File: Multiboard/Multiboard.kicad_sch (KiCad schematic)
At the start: 51 parts, among them J1 Conn_01x20_Socket, J2 Conn_01x20_Socket, J3 Debug, J4 USB_C_Receptacle_USB2.0_16P, SW1 BOOT0, SW2 NRST, SW8 KEY, U1 STM32F411RET6, U2 MAX662AESA_T, U3 MCP1792x-3302xCB, Y1 32.768KHz, Y2 25MHz

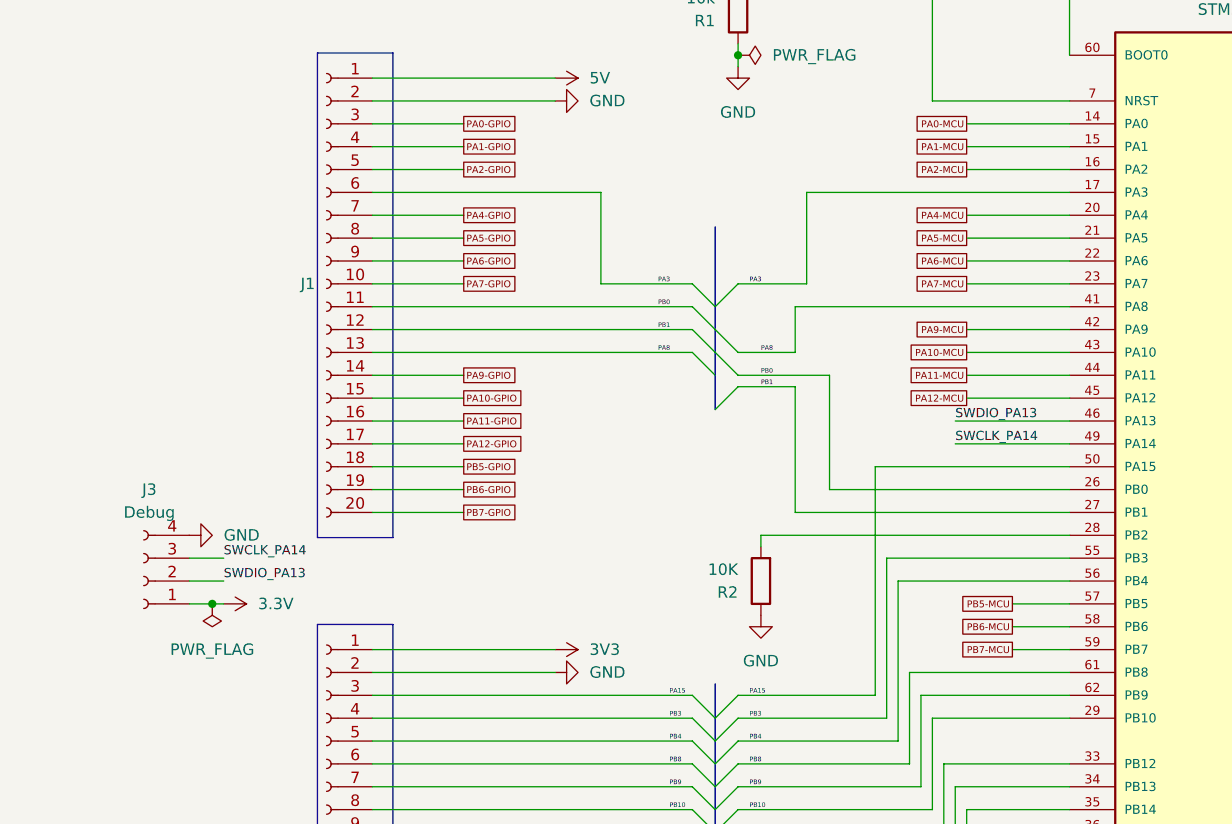
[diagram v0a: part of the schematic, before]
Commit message: FIxed level shifter implementation
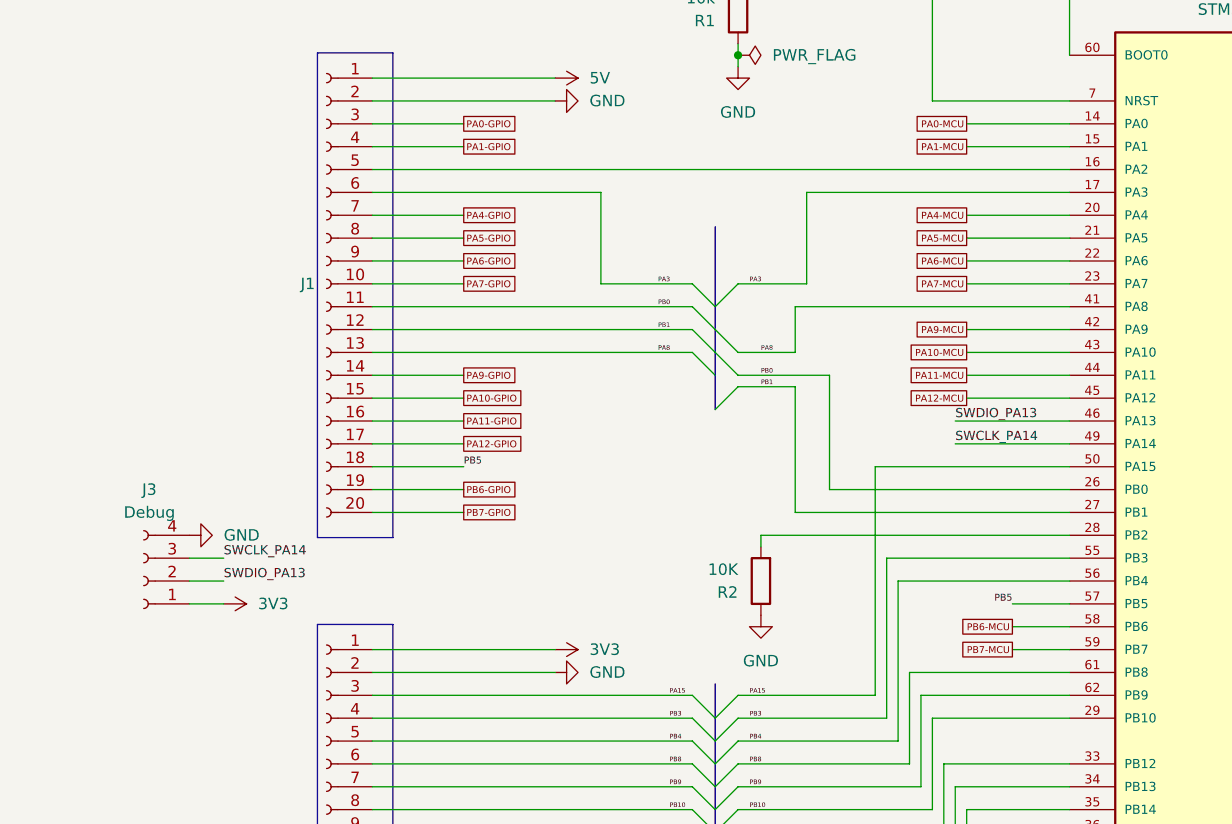
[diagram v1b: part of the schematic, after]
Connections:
- net 3.3V is gone; now on net 3V3: J3.1 (Pin_1)
- net PA2-MCU is gone; now on an unnamed net: U1.16 (PA2)
- net PB5-MCU is gone; now on net PB5: U1.57 (PB5)
- net PA2-GPIO: no longer names the net of J1.5 (Pin_5)
- net PB5-GPIO renamed PB5
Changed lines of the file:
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@@
 	)
 	(junction
-		(at 57.15 123.19)
-		(diameter 0)
-		(color 0 0 0 0)
-	)
-	(junction
 		(at 261.62 83.82)
 		(diameter 0)
@@
 	(wire
 		(pts
-			(xy 74.93 74.93) (xy 85.09 74.93)
+			(xy 74.93 74.93) (xy 152.4 74.93)
 		)
 		(stroke
@@
 	(wire
 		(pts
-			(xy 57.15 123.19) (xy 54.61 123.19)
-		)
-		(stroke
-			(width 0)
-			(type default)
-		)
-	)
-	(wire
-		(pts
 			(xy 74.93 97.79) (xy 85.09 97.79)
 		)
@@
 	(wire
 		(pts
-			(xy 58.42 123.19) (xy 57.15 123.19)
+			(xy 54.61 123.19) (xy 58.42 123.19)
 		)
 		(stroke
@@
 	(wire
 		(pts
-			(xy 140.97 74.93) (xy 152.4 74.93)
-		)
-		(stroke
-			(width 0)
-			(type default)
-		)
-	)
-	(wire
-		(pts
 			(xy 118.11 115.57) (xy 118.11 116.84)
 		)
@@
 		)
 	)
+	(label "PB5"
+		(at 85.09 107.95 0)
+		(effects
+			(font
+				(size 0.762 0.762)
+			)
+			(justify left bottom)
+		)
+	)
 	(label "PB3"
 		(at 107.95 135.89 0)
@@
 		)
 	)
-	(label "PA8"
-		(at 118.11 95.25 0)
-		(effects
-			(font
-				(size 0.508 0.508)
-			)
-			(justify left bottom)
-		)
-	)
-	(global_label "PA2-MCU"
-		(shape passive)
-		(at 140.97 74.93 180)
-		(fields_autoplaced yes)
+	(label "PB5"
+		(at 146.05 123.19 180)
 		(effects
 			(font
 				(size 0.762 0.762)
 			)
-			(justify right)
-		)
-		(property "Intersheetrefs" "${INTERSHEET_REFS}"
-			(at 134.33 74.93 0)
-			(effects
-				(font
-					(size 1.27 1.27)
-				)
-				(justify right)
-				(hide yes)
-			)
+			(justify right bottom)
 		)
 	)
-	(global_label "PB5-GPIO"
-		(shape passive)
-		(at 85.09 107.95 0)
-		(fields_autoplaced yes)
+	(label "PA8"
+		(at 118.11 95.25 0)
 		(effects
 			(font
-				(size 0.762 0.762)
-			)
-			(justify left)
-		)
-		(property "Intersheetrefs" "${INTERSHEET_REFS}"
-			(at 92.0929 107.95 0)
-			(effects
-				(font
-					(size 1.27 1.27)
-				)
-				(justify left)
-				(hide yes)
+				(size 0.508 0.508)
 			)
+			(justify left bottom)
 		)
 	)
@@
 		)
 	)
-	(global_label "PB5-MCU"
-		(shape passive)
-		(at 146.05 123.19 180)
-		(fields_autoplaced yes)
-		(effects
-			(font
-				(size 0.762 0.762)
-			)
-			(justify right)
-		)
-		(property "Intersheetrefs" "${INTERSHEET_REFS}"
-			(at 139.3011 123.19 0)
-			(effects
-				(font
-					(size 1.27 1.27)
-				)
-				(justify right)
-				(hide yes)
-			)
-		)
-	)
 	(global_label "PB6-MCU"
 		(shape passive)
@@
 		)
 	)
-	(global_label "PA2-GPIO"
-		(shape passive)
-		(at 85.09 74.93 0)
-		(fields_autoplaced yes)
-		(effects
-			(font
-				(size 0.762 0.762)
-			)
-			(justify left)
-		)
-		(property "Intersheetrefs" "${INTERSHEET_REFS}"
-			(at 91.984 74.93 0)
-			(effects
-				(font
-					(size 1.27 1.27)
-				)
-				(justify left)
-				(hide yes)
-			)
-		)
-	)
 	(global_label "PC7-MCU"
 		(shape passive)
@@
 	)
 	(symbol
-		(lib_id "power:PWR_FLAG")
-		(at 57.15 123.19 180)
-		(unit 1)
-		(exclude_from_sim no)
-		(in_bom yes)
-		(on_board yes)
-		(dnp no)
-		(fields_autoplaced yes)
-		(property "Reference" "#FLG02"
-			(at 57.15 125.095 0)
-			(effects
-				(font
-					(size 1.27 1.27)
-				)
-				(hide yes)
-			)
-		)
-		(property "Value" "PWR_FLAG"
-			(at 57.15 128.27 0)
-			(effects
-				(font
-					(size 1.27 1.27)
-				)
-			)
-		)
-		(property "Footprint" ""
-			(at 57.15 123.19 0)
-			(effects
-				(font
-					(size 1.27 1.27)
-				)
-				(hide yes)
-			)
-		)
-		(property "Datasheet" "~"
-			(at 57.15 123.19 0)
-			(effects
-				(font
-					(size 1.27 1.27)
-				)
-				(hide yes)
-			)
-		)
-		(property "Description" "Special symbol for telling ERC where power comes from"
-			(at 57.15 123.19 0)
-			(effects
-				(font
-					(size 1.27 1.27)
-				)
-				(hide yes)
-			)
-		)
-		(pin "1"
-		)
-		(instances
-			(project "Multiboard"
-				(path "/9ed4a389-3aa7-41f1-b239-280eb7f09ef1"
-					(reference "#FLG02")
-					(unit 1)
-				)
-			)
-		)
-	)
-	(symbol
 		(lib_id "power:GND")
 		(at 335.28 101.6 0)
@@
 			)
 		)
-		(property "Value" "3.3V"
+		(property "Value" "3V3"
 			(at 62.23 123.1899 90)
 			(effects

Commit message: Fixed bus implementation
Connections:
- net PA15: no longer names the net of J2.3 (Pin_3), U1.50 (PA15)
- net PA3: no longer names the net of J1.6 (Pin_6), U1.17 (PA3)

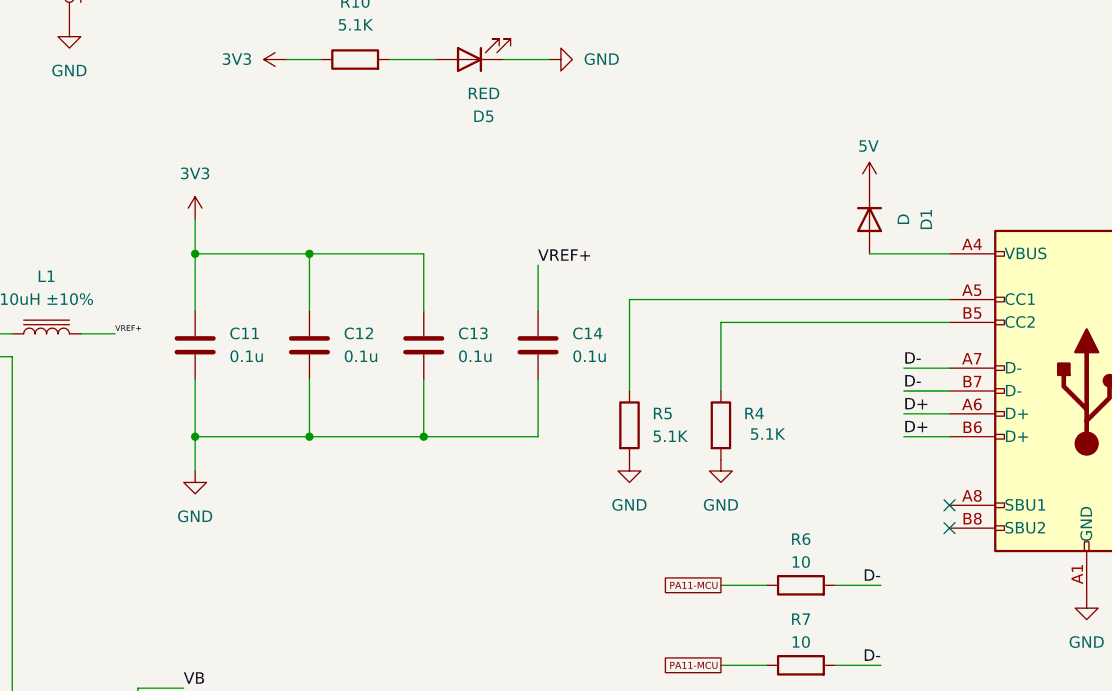
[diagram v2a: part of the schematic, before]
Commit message: positioned USART1 and I2C1 level shifters
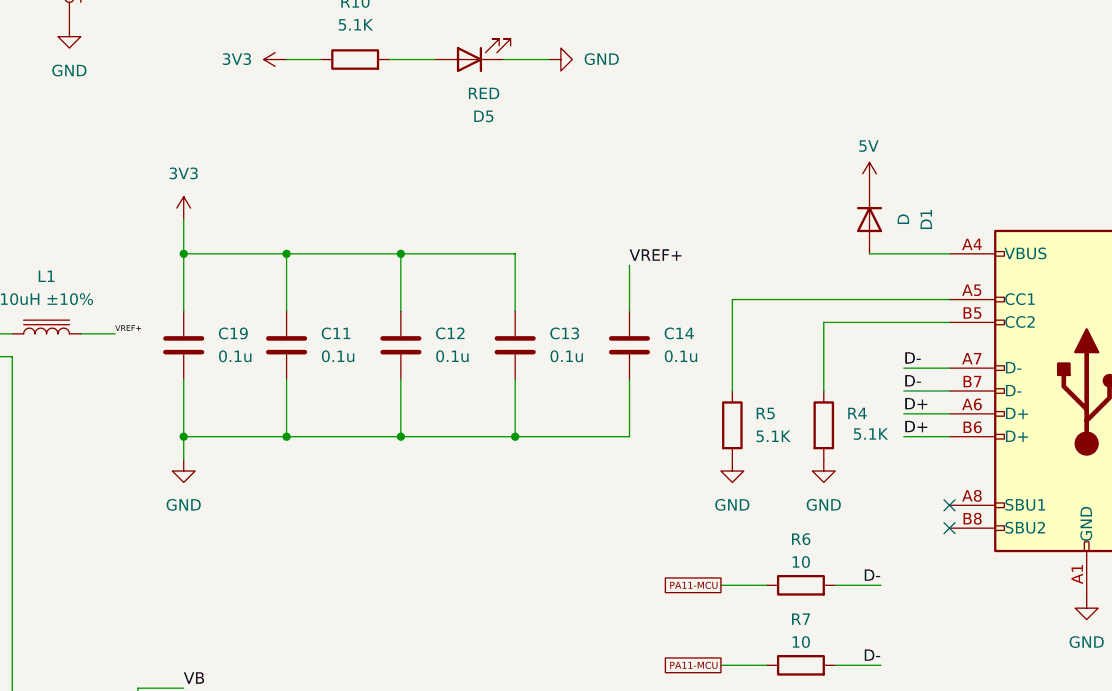
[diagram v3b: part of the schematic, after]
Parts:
- added C19: 0.1u, Capacitor_SMD:C_0603_1608Metric_Pad1.08x0.95mm_HandSolder, symbol Device:C
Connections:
- net 3V3: now also C19.1
- net GND: now also C19.2
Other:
- moved on the sheet: C11, C12, C13, C14, R4, R5

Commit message: wired all level shifters and increased width of decoupling traces
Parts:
- Y1: footprint Crystal:Crystal_SMD_0603-2Pin_6.0x3.5mm_HandSoldering -> Crystal:Crystal_SMD_MicroCrystal_CC7V-T1A-2Pin_3.2x1.5mm_HandSoldering
- Y2: footprint Crystal:Crystal_SMD_0603-2Pin_6.0x3.5mm_HandSoldering -> Crystal:Crystal_SMD_HC49-SD_HandSoldering
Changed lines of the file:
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@@
 			)
 		)
-		(property "Footprint" "Crystal:Crystal_SMD_0603-2Pin_6.0x3.5mm_HandSoldering"
+		(property "Footprint" "Crystal:Crystal_SMD_HC49-SD_HandSoldering"
 			(at 123.19 213.36 0)
 			(effects
@@
 			)
 		)
-		(property "Footprint" "Crystal:Crystal_SMD_0603-2Pin_6.0x3.5mm_HandSoldering"
+		(property "Footprint" "Crystal:Crystal_SMD_MicroCrystal_CC7V-T1A-2Pin_3.2x1.5mm_HandSoldering"
 			(at 123.19 187.96 0)
 			(effects

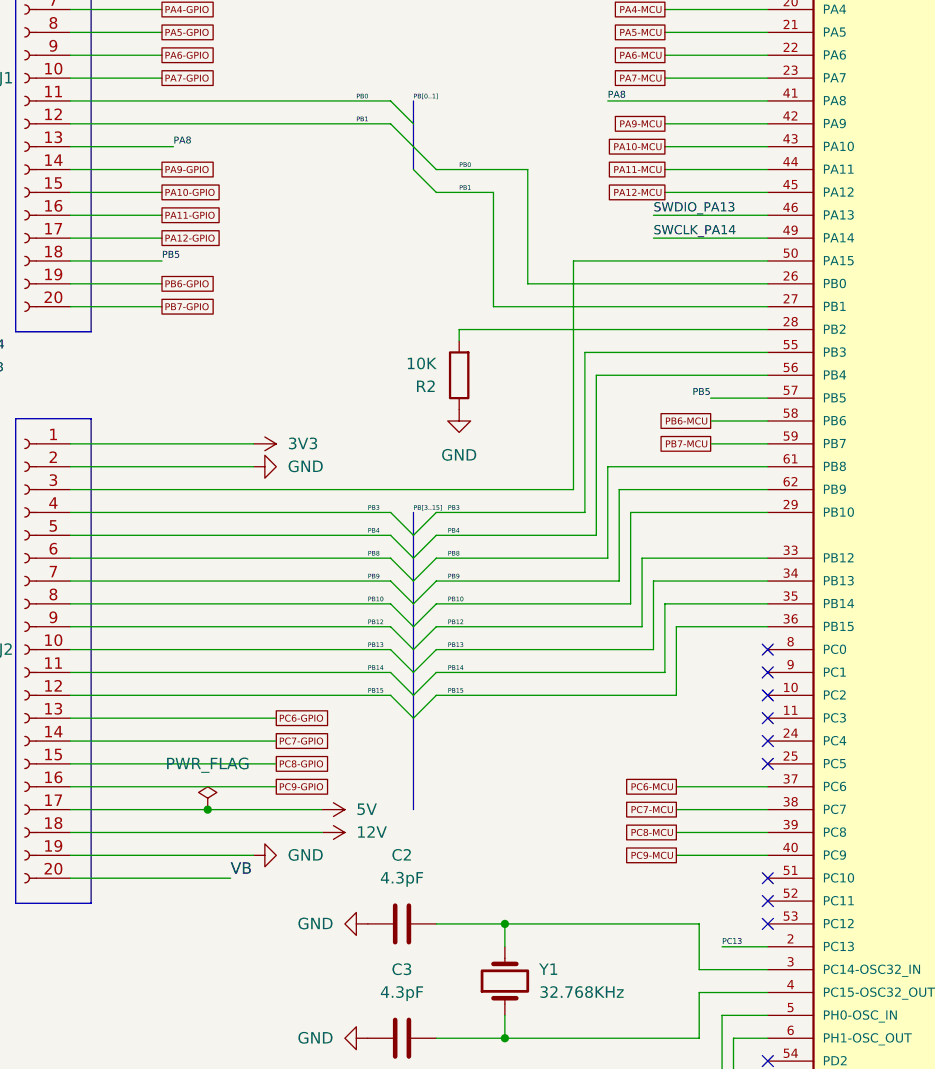
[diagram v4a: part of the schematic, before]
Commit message: wired level shifters; positioed ldo and charge pump
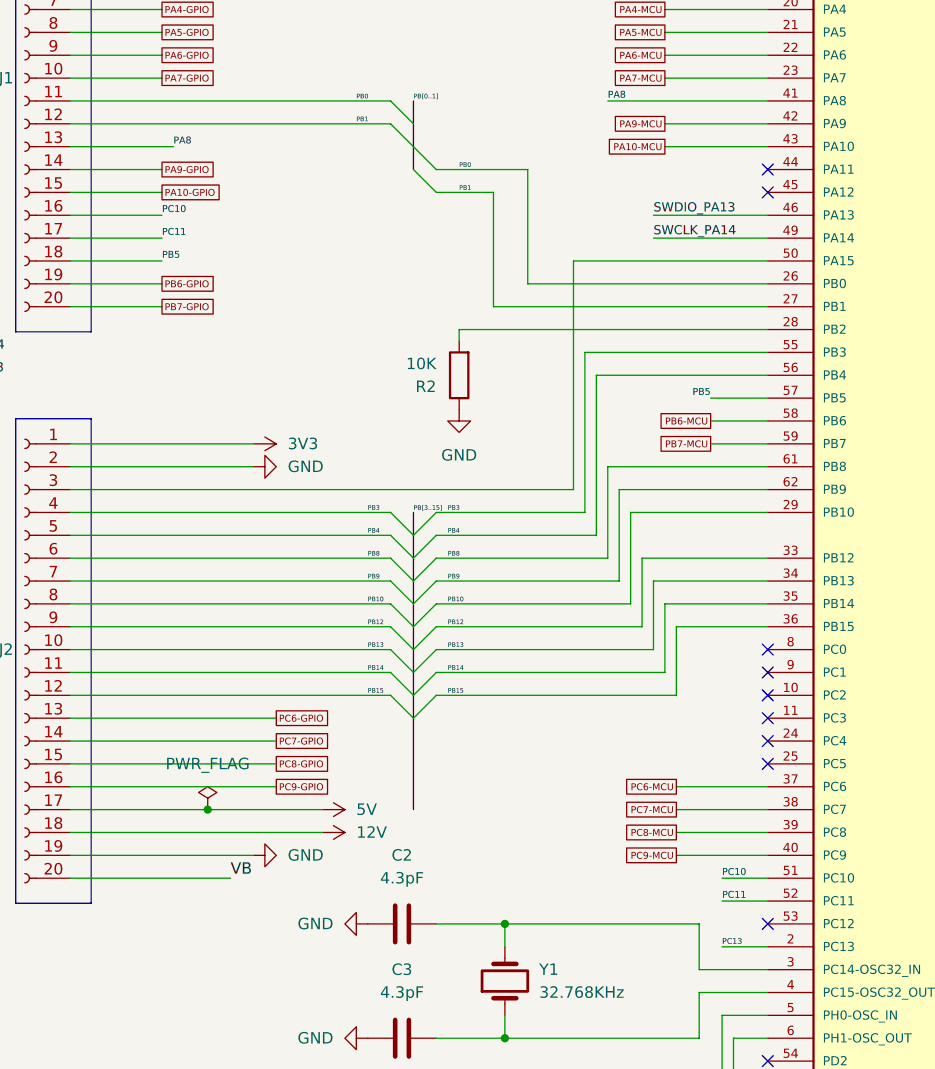
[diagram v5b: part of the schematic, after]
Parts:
- U3: footprint Package_DFN_QFN:DFN-6-1EP_3x3mm_P0.95mm_EP1.7x2.6mm -> Package_TO_SOT_SMD:SOT-23
- Y1: footprint Crystal:Crystal_SMD_MicroCrystal_CC7V-T1A-2Pin_3.2x1.5mm_HandSoldering -> Crystal:Crystal_SMD_3215-2Pin_3.2x1.5mm
- Y2: footprint Crystal:Crystal_SMD_HC49-SD_HandSoldering -> Crystal:Crystal_SMD_HC49-SD
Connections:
- net PA11-GPIO is gone; now on net PC10: J1.16 (Pin_16)
- net PA12-GPIO is gone; now on net PC11: J1.17 (Pin_17)
- net PA11-MCU: no longer U1.44 (PA11)
- net PA12-MCU: no longer U1.45 (PA12)
- net PC10: now reaches U1.51 (PC10)
- net PC11: now reaches U1.52 (PC11)
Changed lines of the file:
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@@
 	)
 	(no_connect
-		(at 152.4 176.53)
-	)
-	(no_connect
 		(at 320.04 93.98)
 	)
@@
 	)
 	(no_connect
-		(at 152.4 151.13)
+		(at 152.4 97.79)
 	)
 	(no_connect
-		(at 152.4 158.75)
+		(at 152.4 100.33)
 	)
 	(no_connect
-		(at 152.4 179.07)
+		(at 152.4 151.13)
+	)
+	(no_connect
+		(at 152.4 158.75)
 	)
 	(no_connect
@@
 	(wire
 		(pts
-			(xy 140.97 100.33) (xy 152.4 100.33)
-		)
-		(stroke
-			(width 0)
-			(type default)
-		)
-	)
-	(wire
-		(pts
 			(xy 246.38 83.82) (xy 259.08 83.82)
 		)
@@
 	(wire
 		(pts
+			(xy 147.32 176.53) (xy 152.4 176.53)
+		)
+		(stroke
+			(width 0)
+			(type default)
+		)
+	)
+	(wire
+		(pts
 			(xy 74.93 153.67) (xy 110.49 153.67)
 		)
@@
 	(wire
 		(pts
-			(xy 140.97 97.79) (xy 152.4 97.79)
+			(xy 140.97 69.85) (xy 152.4 69.85)
 		)
 		(stroke
@@
 	(wire
 		(pts
-			(xy 140.97 69.85) (xy 152.4 69.85)
+			(xy 299.72 170.18) (xy 340.36 170.18)
 		)
 		(stroke
@@
 	(wire
 		(pts
-			(xy 299.72 170.18) (xy 340.36 170.18)
+			(xy 284.48 64.77) (xy 284.48 69.85)
 		)
 		(stroke
@@
 	(wire
 		(pts
-			(xy 284.48 64.77) (xy 284.48 69.85)
+			(xy 195.58 69.85) (xy 207.01 69.85)
 		)
 		(stroke
@@
 	(wire
 		(pts
-			(xy 195.58 69.85) (xy 207.01 69.85)
+			(xy 152.4 133.35) (xy 135.89 133.35)
 		)
 		(stroke
@@
 	(wire
 		(pts
-			(xy 152.4 133.35) (xy 135.89 133.35)
+			(xy 152.4 53.34) (xy 152.4 62.23)
 		)
 		(stroke
@@
 	(wire
 		(pts
-			(xy 152.4 53.34) (xy 152.4 62.23)
+			(xy 147.32 179.07) (xy 152.4 179.07)
 		)
 		(stroke
@@
 		)
 	)
+	(label "PC10"
+		(at 85.09 102.87 0)
+		(effects
+			(font
+				(size 0.762 0.762)
+			)
+			(justify left bottom)
+		)
+	)
 	(label "SWDIO_PA13"
 		(at 139.7 102.87 0)
@@
 		)
 	)
+	(label "PC11"
+		(at 147.32 179.07 0)
+		(effects
+			(font
+				(size 0.762 0.762)
+			)
+			(justify left bottom)
+		)
+	)
 	(label "PC13"
 		(at 276.86 25.4 0)
@@
 		)
 	)
+	(label "PC11"
+		(at 85.09 105.41 0)
+		(effects
+			(font
+				(size 0.762 0.762)
+			)
+			(justify left bottom)
+		)
+	)
 	(label "D+"
 		(at 314.96 81.28 0)
@@
 		)
 	)
+	(label "PC10"
+		(at 147.32 176.53 0)
+		(effects
+			(font
+				(size 0.762 0.762)
+			)
+			(justify left bottom)
+		)
+	)
 	(label "PB14"
 		(at 107.95 153.67 0)
@@
 		)
 	)
-	(global_label "PA12-MCU"
-		(shape passive)
-		(at 140.97 100.33 180)
-		(fields_autoplaced yes)
-		(effects
-			(font
-				(size 0.762 0.762)
-			)
-			(justify right)
-		)
-		(property "Intersheetrefs" "${INTERSHEET_REFS}"
-			(at 133.6043 100.33 0)
-			(effects
-				(font
-					(size 1.27 1.27)
-				)
-				(justify right)
-				(hide yes)
-			)
-		)
-	)
 	(global_label "PA11-MCU"
 		(shape passive)
@@
 		)
 	)
-	(global_label "PA12-GPIO"
-		(shape passive)
-		(at 85.09 105.41 0)
-		(fields_autoplaced yes)
-		(effects
-			(font
-				(size 0.762 0.762)
-			)
-			(justify left)
-		)
-		(property "Intersheetrefs" "${INTERSHEET_REFS}"
-			(at 92.7097 105.41 0)
-			(effects
-				(font
-					(size 1.27 1.27)
-				)
-				(justify left)
-				(hide yes)
-			)
-		)
-	)
 	(global_label "PA4-GPIO"
 		(shape passive)
@@
 		)
 	)
-	(global_label "PA11-GPIO"
-		(shape passive)
-		(at 85.09 102.87 0)
-		(fields_autoplaced yes)
-		(effects
-			(font
-				(size 0.762 0.762)
-			)
-			(justify left)
-		)
-		(property "Intersheetrefs" "${INTERSHEET_REFS}"
-			(at 92.7097 102.87 0)
-			(effects
-				(font
-					(size 1.27 1.27)
-				)
-				(justify left)
-				(hide yes)
-			)
-		)
-	)
 	(global_label "PC6-MCU"
 		(shape passive)
@@
 		)
 	)
-	(global_label "PA11-MCU"
-		(shape passive)
-		(at 140.97 97.79 180)
-		(fields_autoplaced yes)
-		(effects
-			(font
-				(size 0.762 0.762)
-			)
-			(justify right)
-		)
-		(property "Intersheetrefs" "${INTERSHEET_REFS}"
-			(at 133.6043 97.79 0)
-			(effects
-				(font
-					(size 1.27 1.27)
-				)
-				(justify right)
-				(hide yes)
-			)
-		)
-	)
 	(symbol
 		(lib_id "power:GND")
@@
 			)
 		)
-		(property "Footprint" "Package_DFN_QFN:DFN-6-1EP_3x3mm_P0.95mm_EP1.7x2.6mm"
+		(property "Footprint" "Package_TO_SOT_SMD:SOT-23"
 			(at 345.44 120.015 0)
 			(effects
@@
 			)
 		)
-		(property "Footprint" "Crystal:Crystal_SMD_HC49-SD_HandSoldering"
+		(property "Footprint" "Crystal:Crystal_SMD_HC49-SD"
 			(at 123.19 213.36 0)
 			(effects
@@
 			)
 		)
-		(property "Footprint" "Crystal:Crystal_SMD_MicroCrystal_CC7V-T1A-2Pin_3.2x1.5mm_HandSoldering"
+		(property "Footprint" "Crystal:Crystal_SMD_3215-2Pin_3.2x1.5mm"
 			(at 123.19 187.96 0)
 			(effects
